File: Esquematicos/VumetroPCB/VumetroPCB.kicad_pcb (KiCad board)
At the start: 2 copper layers, 104.1 x 144.8 mm, 27 parts, among them J1 AudioJack, P1 Pin_Puente, P10 Pin_Puente, P2 Pin_Puente, P3 Pin_Puente, P4 Pin_Puente, P5 Pin_Puente, P6 Pin_Puente, P7 Pin_Puente, P8 Pin_Puente, P9 Pin_Puente, U1 conn_teclado_4x4, U2 opa2350pa, U3 MAX7219, U4 MatrixLed8x8

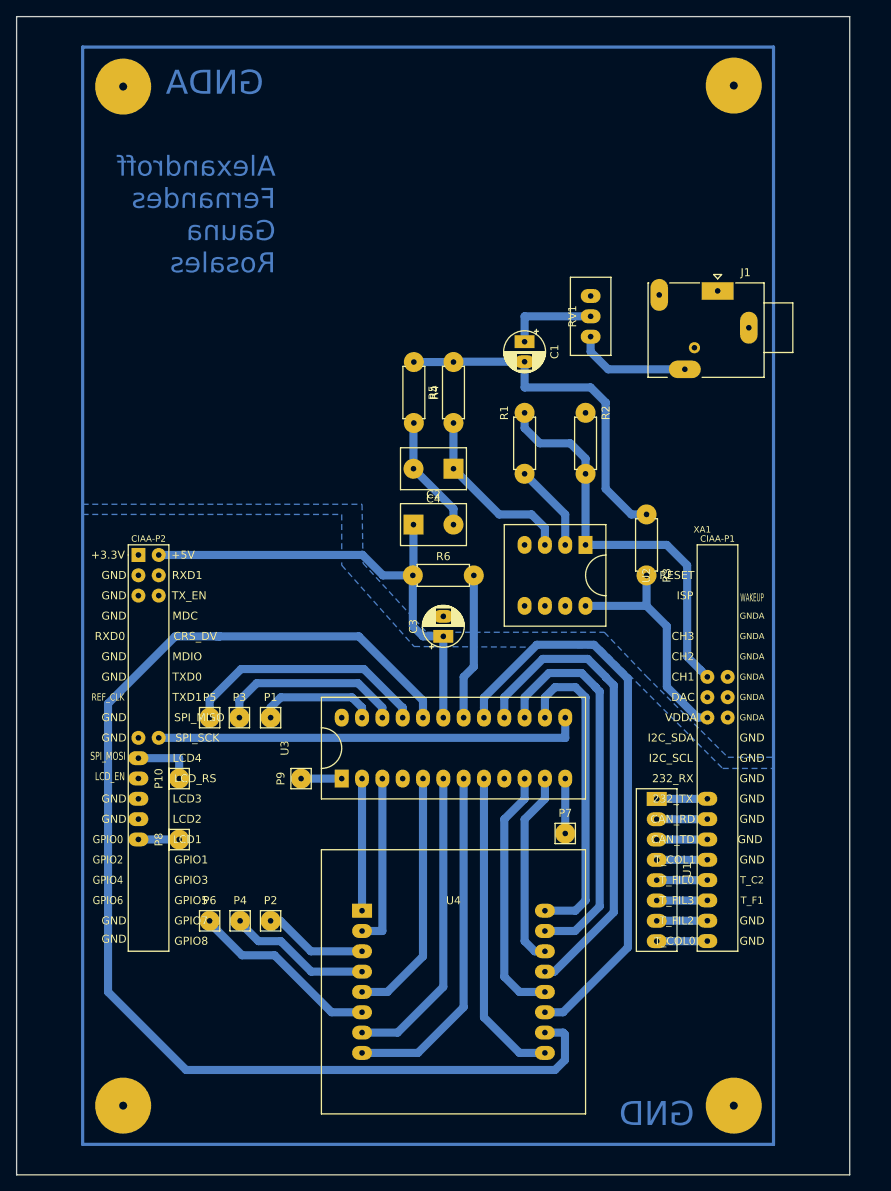
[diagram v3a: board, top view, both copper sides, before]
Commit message: Arreglo de los errores de diseño en la PCB
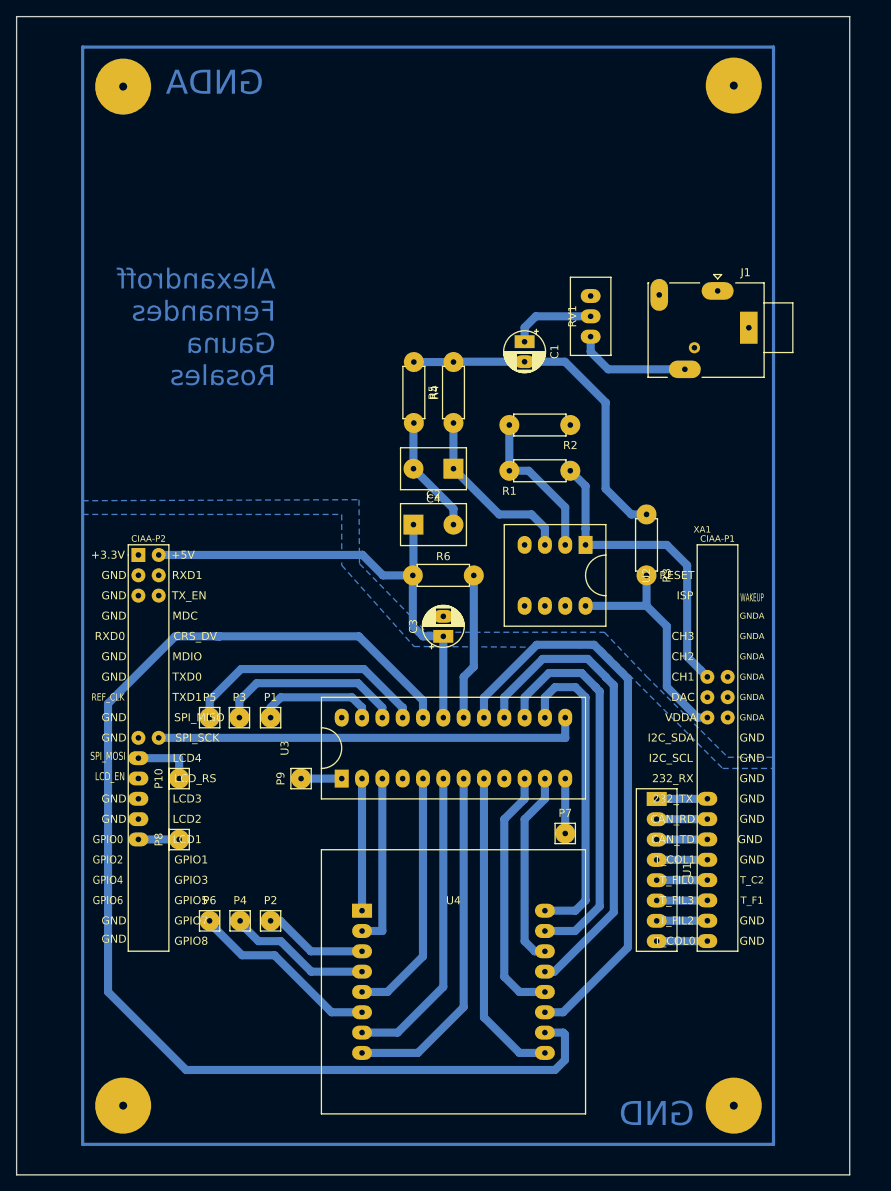
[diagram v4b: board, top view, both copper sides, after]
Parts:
- C4: value 1.8nF -> 2.2nF
- moved R2 11.3 mm to (117.5, 65.0), turned to 0 degrees
- moved R1 5.73 mm to (125.1, 70.7), turned to 180 degrees
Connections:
- R1 pad 1: Net-(R1-Pad1) -> /CH1
- R1 pad 2: /CH1 -> Net-(R1-Pad2)
- R2 pad 1: /CH1 -> Net-(R1-Pad2)
- U2 pad 2: Net-(R1-Pad1) -> Net-(R1-Pad2)
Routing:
- net Net-(R1-Pad2): track 0.00 -> 19.3 mm
- net /CH1: track 50.7 -> 38.8 mm
- net Net-(R1-Pad1): track 11.0 -> 0.00 mm
- net Net-(C1-Pad2): track 45.2 -> 43.4 mm
- net Net-(C1-Pad1): track 11.4 -> 10.6 mm
